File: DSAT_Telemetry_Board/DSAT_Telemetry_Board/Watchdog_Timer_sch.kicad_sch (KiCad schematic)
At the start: 4 parts

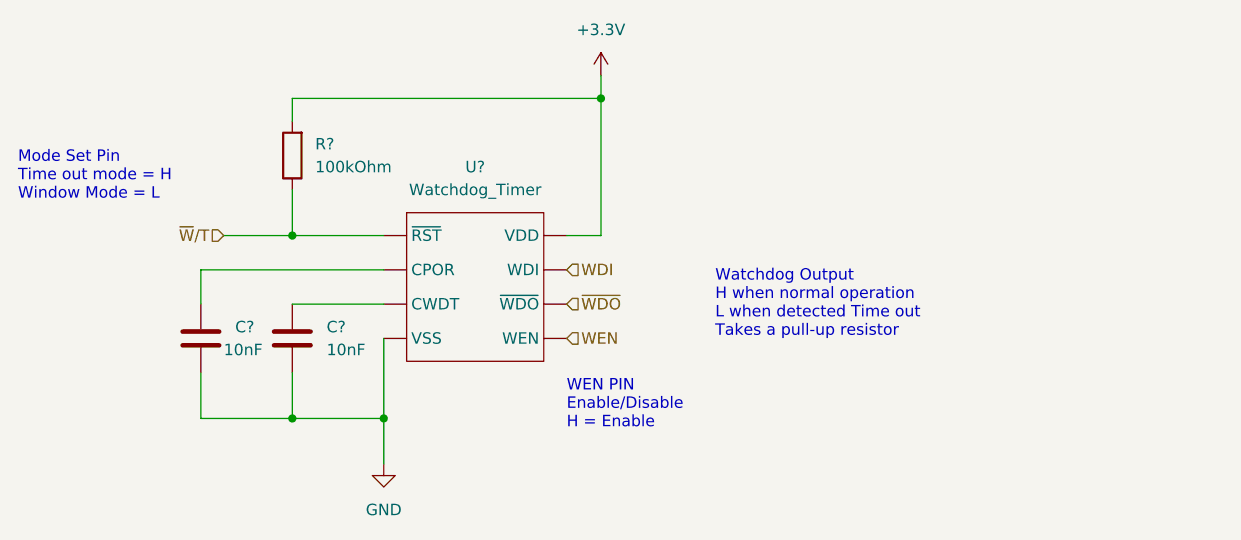
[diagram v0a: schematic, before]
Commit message: Added Transciever Updates/Biases/RF_Switch
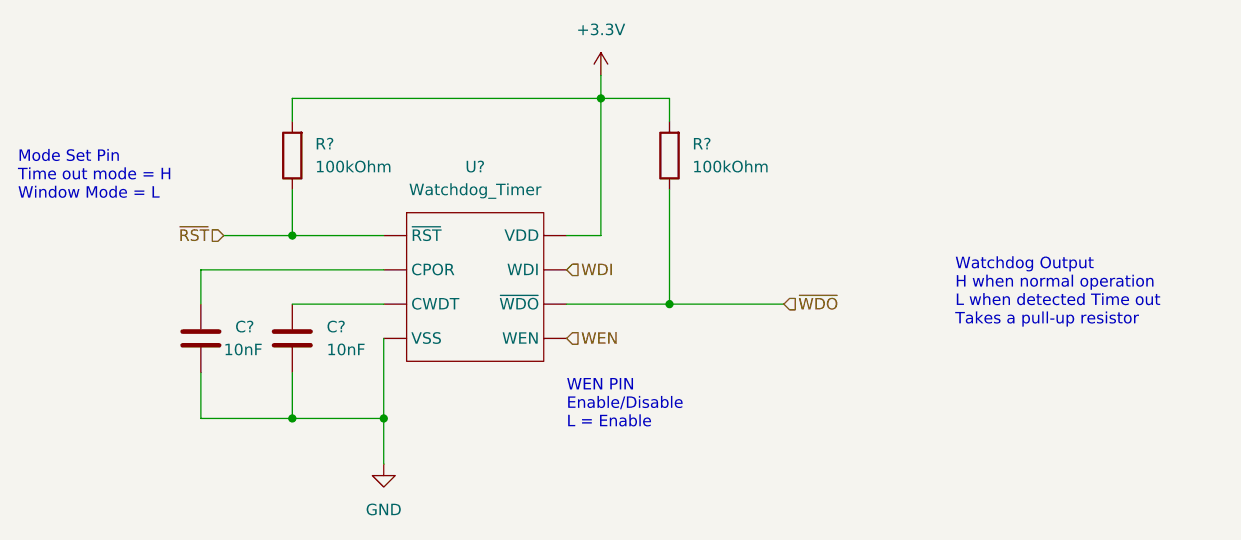
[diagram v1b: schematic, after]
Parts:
- added R?: 100kOhm, symbol Device:R
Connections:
- net +3V3: now also R?.2
- net ~{WDO}: now also R?.1
- net ~{W}/T renamed ~{RST}
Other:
- note added: "WEN PIN Enable/Disable L = Enable"
- note removed: "WEN PIN Enable/Disable H = Enable"
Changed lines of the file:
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@@
   (junction (at 143.51 54.61) (diameter 0) (color 0 0 0 0)
+  )
+  (junction (at 151.13 77.47) (diameter 0) (color 0 0 0 0)
   )
   (junction (at 109.22 90.17) (diameter 0) (color 0 0 0 0)
@@
     (stroke (width 0) (type default) (color 0 0 0 0))
   )
+  (wire (pts (xy 143.51 54.61) (xy 151.13 54.61))
+    (stroke (width 0) (type default) (color 0 0 0 0))
+  )
   (wire (pts (xy 99.06 90.17) (xy 99.06 85.09))
     (stroke (width 0) (type default) (color 0 0 0 0))
@@
   )
   (wire (pts (xy 119.38 73.66) (xy 99.06 73.66))
+    (stroke (width 0) (type default) (color 0 0 0 0))
+  )
+  (wire (pts (xy 163.83 77.47) (xy 151.13 77.47))
     (stroke (width 0) (type default) (color 0 0 0 0))
   )
@@
     (stroke (width 0) (type default) (color 0 0 0 0))
   )
+  (wire (pts (xy 151.13 54.61) (xy 151.13 57.15))
+    (stroke (width 0) (type default) (color 0 0 0 0))
+  )
+  (wire (pts (xy 151.13 64.77) (xy 151.13 77.47))
+    (stroke (width 0) (type default) (color 0 0 0 0))
+  )
   (wire (pts (xy 109.22 90.17) (xy 119.38 90.17))
+    (stroke (width 0) (type default) (color 0 0 0 0))
+  )
+  (wire (pts (xy 151.13 77.47) (xy 139.7 77.47))
     (stroke (width 0) (type default) (color 0 0 0 0))
   )
@@
     (stroke (width 0) (type default) (color 0 0 0 0))
   )
-  (text "WEN PIN\nEnable/Disable\nH = Enable\n" (at 139.7 91.44 0)
+  (text "WEN PIN\nEnable/Disable\nL = Enable\n" (at 139.7 91.44 0)
     (effects (font (size 1.27 1.27)) (justify left bottom))
   )
   (text "Watchdog Output \nH when normal operation\nL when detected Time out\nTakes a pull-up resistor\n"
-    (at 156.21 81.28 0)
+    (at 182.88 80.01 0)
     (effects (font (size 1.27 1.27)) (justify left bottom))
   )
@@
     (effects (font (size 1.27 1.27)) (justify left bottom))
   )
-  (hierarchical_label "~{W}{slash}T" (shape input) (at 101.6 69.85 180)
+  (hierarchical_label "~{RST}" (shape input) (at 101.6 69.85 180)
     (effects (font (size 1.27 1.27)) (justify right))
   )
@@
     (effects (font (size 1.27 1.27)) (justify left))
   )
-  (hierarchical_label "~{WDO}" (shape input) (at 139.7 77.47 0)
+  (hierarchical_label "~{WDO}" (shape input) (at 163.83 77.47 0)
     (effects (font (size 1.27 1.27)) (justify left))
   )
@@
     (pin "1")
   )
+  (symbol (lib_id "Device:R") (at 151.13 60.96 180) (unit 1)
+    (in_bom yes) (on_board yes) (fields_autoplaced)
+    (property "Reference" "R?" (id 0) (at 153.67 59.6899 0)
+      (effects (font (size 1.27 1.27)) (justify right))
+    )
+    (property "Value" "100kOhm" (id 1) (at 153.67 62.2299 0)
+      (effects (font (size 1.27 1.27)) (justify right))
+    )
+    (property "Footprint" "" (id 2) (at 152.908 60.96 90)
+      (effects (font (size 1.27 1.27)) hide)
+    )
+    (property "Datasheet" "~" (id 3) (at 151.13 60.96 0)
+      (effects (font (size 1.27 1.27)) hide)
+    )
+    (pin "1")
+    (pin "2")
+  )
   (symbol (lib_id "Device:R") (at 109.22 60.96 180) (unit 1)
